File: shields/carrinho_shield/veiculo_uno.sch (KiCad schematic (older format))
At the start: 29 parts, among them J1 Conn_01x26_Male, J10 Conn_01x02_Male, J11 Conn_01x02_Male, J12 Conn_01x02_Male, J13 Conn_01x02_Male, J14 Conn_01x02_Male, J15 Conn_01x02_Male, J16 Conn_01x02_Male, J17 Conn_01x02_Male, J18 Conn_01x02_Male, J19 Conn_01x02_Male, J2 Conn_01x02_Male, J20 Conn_01x02_Male, J21 Conn_01x02_Male, J3 Conn_01x02_Male, J4 Conn_01x02_Male, J5 Conn_01x02_Male, J6 Conn_01x02_Male, J7 Conn_01x02_Male, J8 Conn_01x02_Male, J9 Conn_01x02_Male, P1 Power, P2 Analog, P3 Digital, P4 Digital, P5 CONN_01X01, P6 CONN_01X01, P7 CONN_01X01, P8 CONN_01X01

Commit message: Added shield schematic
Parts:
- removed J1: Conn_01x26_Male, Connector_PinSocket_2.54mm:PinSocket_2x13_P2.54mm_Vertical, symbol Connector:Conn_01x26_Male
- removed J7: Conn_01x02_Male, Connector_PinHeader_2.54mm:PinHeader_1x02_P2.54mm_Vertical, symbol Connector:Conn_01x02_Male
- added C1, C2: 100n, Capacitor_SMD:C_0805_2012Metric_Pad1.15x1.40mm_HandSolder, symbol pspice:CAP
- added J23: Conn_01x04_Male, Connector_PinHeader_2.54mm:PinHeader_1x04_P2.54mm_Vertical, symbol Connector:Conn_01x04_Male
- added J6: Conn_01x02_Male, Connector_PinHeader_2.54mm:PinHeader_1x02_P2.54mm_Vertical, symbol Connector:Conn_01x02_Male
- added J7: Conn_02x13_Odd_Even, Connector_PinSocket_2.54mm:PinSocket_2x13_P2.54mm_Vertical, symbol Connector_Generic:Conn_02x13_Odd_Even
- renumbered J11 to J1, J2 to J10, J4 to J11, J10 to J12, J14 to J13, J18 to J14, J19 to J16, J12 to J17, J16 to J18, J13 to J19, J5 to J2, J17 to J20, J20 to J3, J6 to J4, J8 to J5, J3 to J8
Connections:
- net labels added: AMP1, AMP2
- net labels removed: A1', A2', Conector, Conector'
- wire segments 121 -> 156
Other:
- note added: "11 - OC2A\n3 - OC2B\n\n6 - OC0A\n5- OC0B"
- note added: "2 - int0 (ext. event)\n8 - ICP1 (capture)\n\n4 - GPIO\n7 - GPIO"
- note added: "Encoder"
- moved on the sheet: J1, J10, J11, J12, J13, J14, J15, J16, J17, J18, J19, J2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

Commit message: Done PCI layout
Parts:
- removed P5: CONN_01X01, Socket_Arduino_Uno:Arduino_1pin, symbol Connector_Generic:Conn_01x01
- added D1: LED, LED_SMD:LED_0805_2012Metric, symbol Device:LED
- added R1: R, Resistor_SMD:R_0805_2012Metric, symbol Device:R
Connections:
- net +5V: now also D1.2 (A)
- net A0: now also J3.2 (Pin_2); no longer J1.2 (Pin_2)
- net A2: now also J1.2 (Pin_2); no longer J3.2 (Pin_2)
- net GND: now also J7.18 (Pin_18), R1.2
- new net: D1.1 (K), R1.1
- no-connect marks 5 -> 4
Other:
- note added: "SHIELD ARDUINO PARA CARRINHO AUTÔNOMO\nLIGAÇÃO CONFORME PLACA DE POTÊNCIA"
- note added: "Sensor optico"
- moved on the sheet: J10, J11, J12, J13, J14, J15, J16, J17, J18, J19, J20, J21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

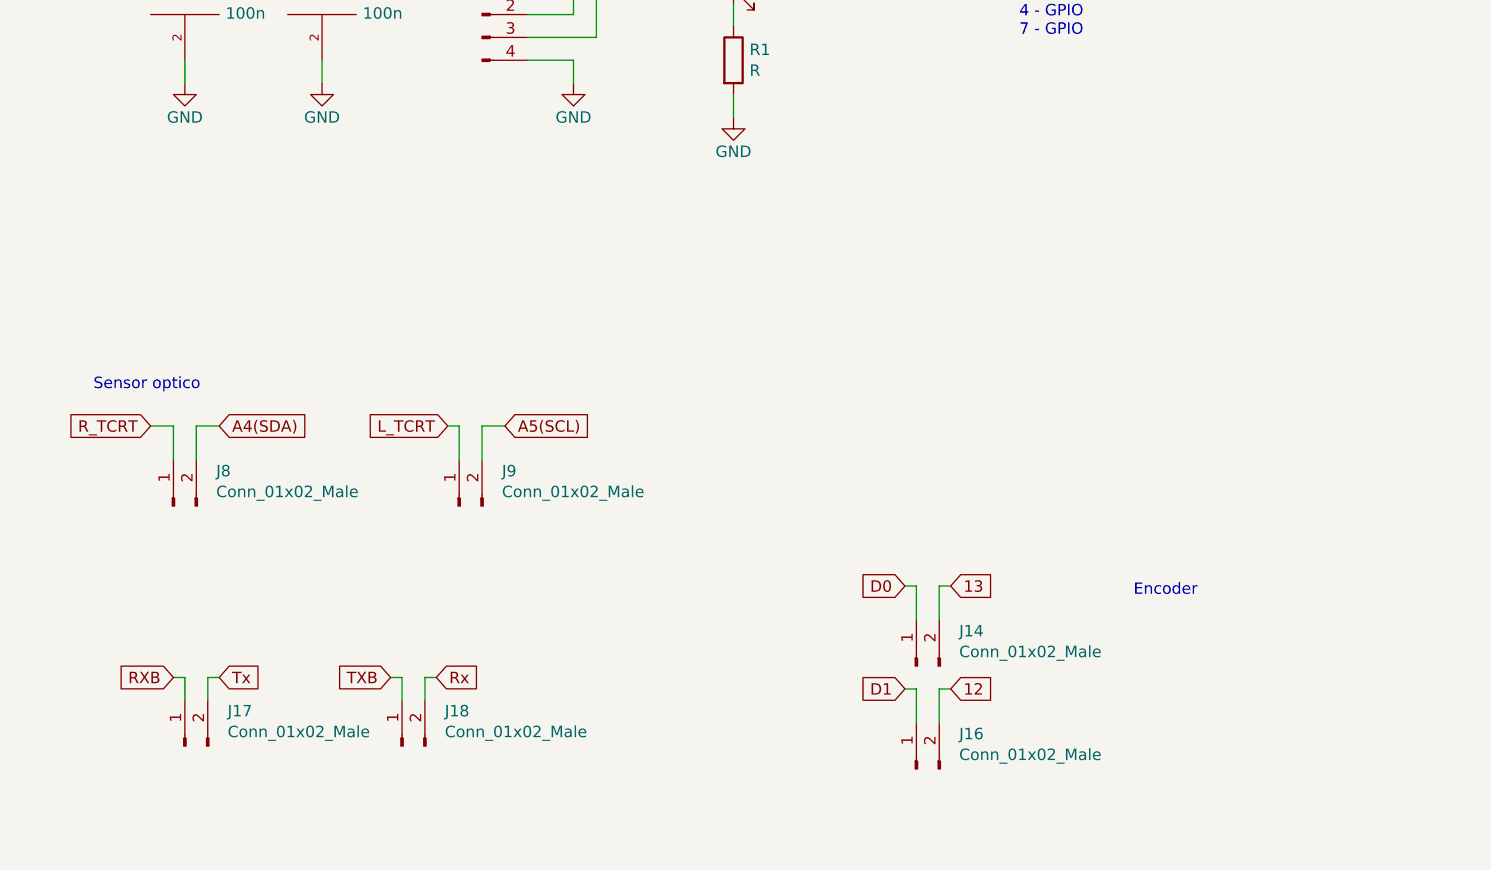
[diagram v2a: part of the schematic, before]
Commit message: Added level converter RX / TX signals
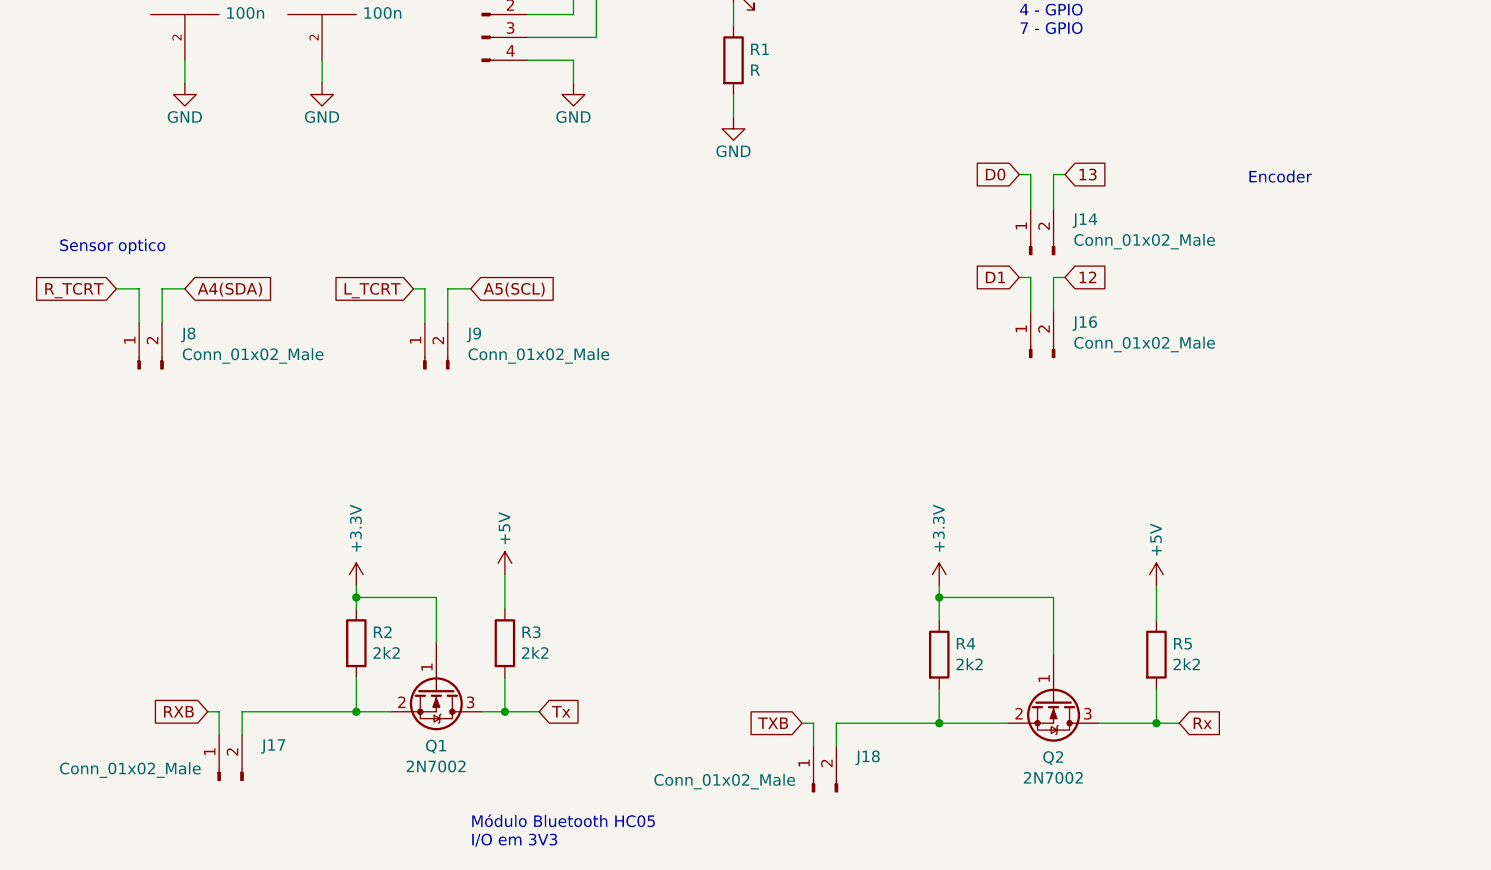
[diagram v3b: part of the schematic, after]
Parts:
- added Q1, Q2: 2N7002, Package_TO_SOT_SMD:SOT-23, symbol Transistor_FET:2N7002
- added R2, R3, R4, R5: 2k2, Resistor_SMD:R_0805_2012Metric, symbol Device:R
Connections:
- net +3V3: now also Q1.1 (G), Q2.1 (G), R2.1, R4.1
- net +5V: now also R3.1, R5.1
- net Rx: now also Q2.3 (D), R5.2; no longer J18.2 (Pin_2)
- net Tx: now also Q1.3 (D), R3.2; no longer J17.2 (Pin_2)
- new net: J18.2 (Pin_2), Q2.2 (S), R4.2
- new net: J17.2 (Pin_2), Q1.2 (S), R2.2
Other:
- note added: "Módulo Bluetooth HC05\nI/O em 3V3"
- moved on the sheet: J14, J16, J17, J18, J8, J9

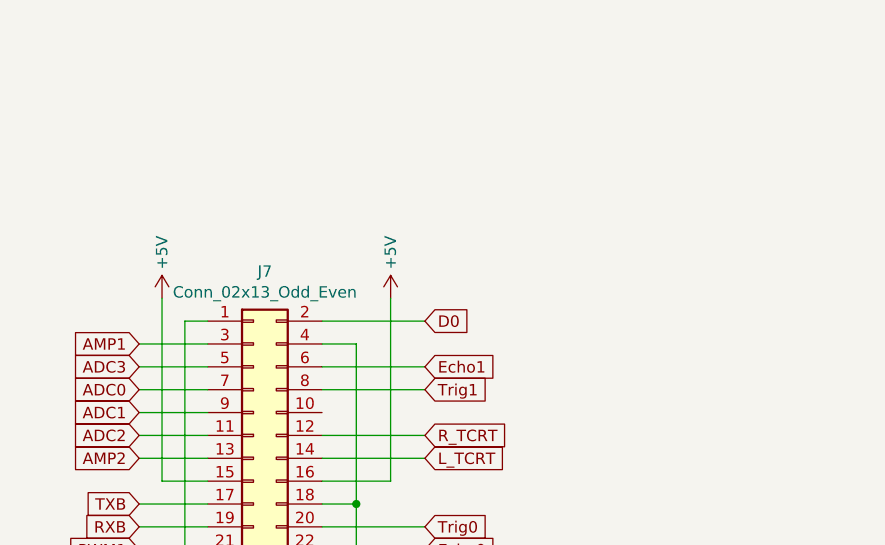
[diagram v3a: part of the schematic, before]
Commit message: Added diode in +5V.
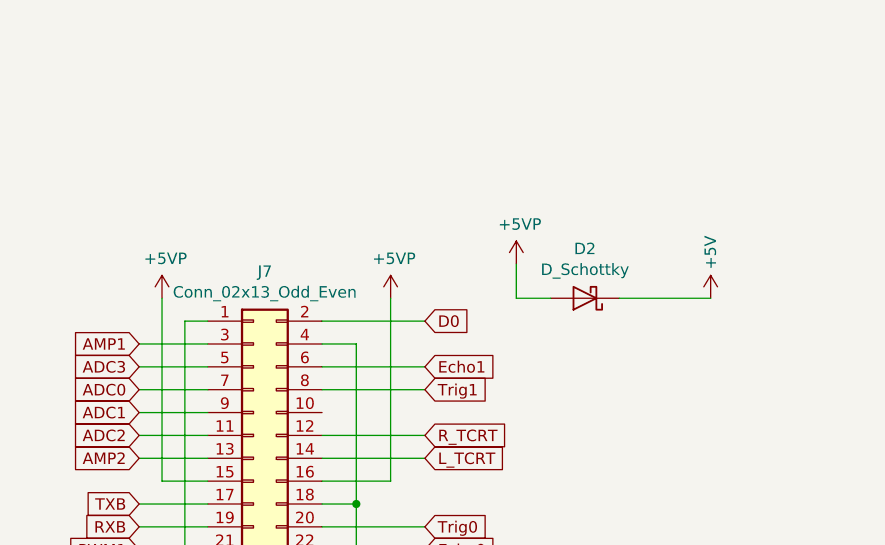
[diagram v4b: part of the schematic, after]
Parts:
- added D2: D_Schottky, Diode_SMD:D_SMB, symbol Device:D_Schottky
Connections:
- net +5V: now also D2.1 (K); no longer J7.15 (Pin_15), J7.16 (Pin_16)
- new net +5VP: D2.2 (A), J7.15 (Pin_15), J7.16 (Pin_16)
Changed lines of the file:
@@
 Wire Wire Line
 	2250 1850 2250 2550
-$Comp
-L power:+5V #PWR05
-U 1 1 5EE2252F
-P 1400 1650
-F 0 "#PWR05" H 1400 1500 50  0001 C CNN
-F 1 "+5V" V 1400 1850 50  0000 C CNN
-F 2 "" H 1400 1650 50  0000 C CNN
-F 3 "" H 1400 1650 50  0000 C CNN
-	1    1400 1650
-	1    0    0    -1
-$EndComp
-$Comp
-L power:+5V #PWR06
-U 1 1 5EE2270A
-P 2400 1650
-F 0 "#PWR06" H 2400 1500 50  0001 C CNN
-F 1 "+5V" V 2400 1850 50  0000 C CNN
-F 2 "" H 2400 1650 50  0000 C CNN
-F 3 "" H 2400 1650 50  0000 C CNN
-	1    2400 1650
-	1    0    0    -1
-$EndComp
 Wire Wire Line
 	2100 2450 2400 2450
@@
 Text Notes 2750 7700 0    50   ~ 0
 Módulo Bluetooth HC05\nI/O em 3V3
+$Comp
+L power:+5VP #PWR06
+U 1 1 5F931DB6
+P 2400 1650
+F 0 "#PWR06" H 2400 1500 50  0001 C CNN
+F 1 "+5VP" H 2415 1823 50  0000 C CNN
+F 2 "" H 2400 1650 50  0001 C CNN
+F 3 "" H 2400 1650 50  0001 C CNN
+	1    2400 1650
+	1    0    0    -1
+$EndComp
+$Comp
+L power:+5VP #PWR05
+U 1 1 5F931E0F
+P 1400 1650
+F 0 "#PWR05" H 1400 1500 50  0001 C CNN
+F 1 "+5VP" H 1415 1823 50  0000 C CNN
+F 2 "" H 1400 1650 50  0001 C CNN
+F 3 "" H 1400 1650 50  0001 C CNN
+	1    1400 1650
+	1    0    0    -1
+$EndComp
+$Comp
+L power:+5VP #PWR015
+U 1 1 5F9467DA
+P 2950 1500
+F 0 "#PWR015" H 2950 1350 50  0001 C CNN
+F 1 "+5VP" H 2965 1673 50  0000 C CNN
+F 2 "" H 2950 1500 50  0001 C CNN
+F 3 "" H 2950 1500 50  0001 C CNN
+	1    2950 1500
+	1    0    0    -1
+$EndComp
+$Comp
+L power:+5V #PWR016
+U 1 1 5F946885
+P 3800 1650
+F 0 "#PWR016" H 3800 1500 50  0001 C CNN
+F 1 "+5V" V 3800 1850 50  0000 C CNN
+F 2 "" H 3800 1650 50  0000 C CNN
+F 3 "" H 3800 1650 50  0000 C CNN
+	1    3800 1650
+	1    0    0    -1
+$EndComp
+$Comp
+L Device:D_Schottky D2
+U 1 1 5F967836
+P 3250 1650
+F 0 "D2" H 3250 1434 50  0000 C CNN
+F 1 "D_Schottky" H 3250 1525 50  0000 C CNN
+F 2 "Diode_SMD:D_SMB" H 3250 1650 50  0001 C CNN
+F 3 "~" H 3250 1650 50  0001 C CNN
+	1    3250 1650
+	-1   0    0    1
+$EndComp
+Wire Wire Line
+	3100 1650 2950 1650
+Wire Wire Line
+	2950 1650 2950 1500
+Wire Wire Line
+	3400 1650 3800 1650
 $EndSCHEMATC

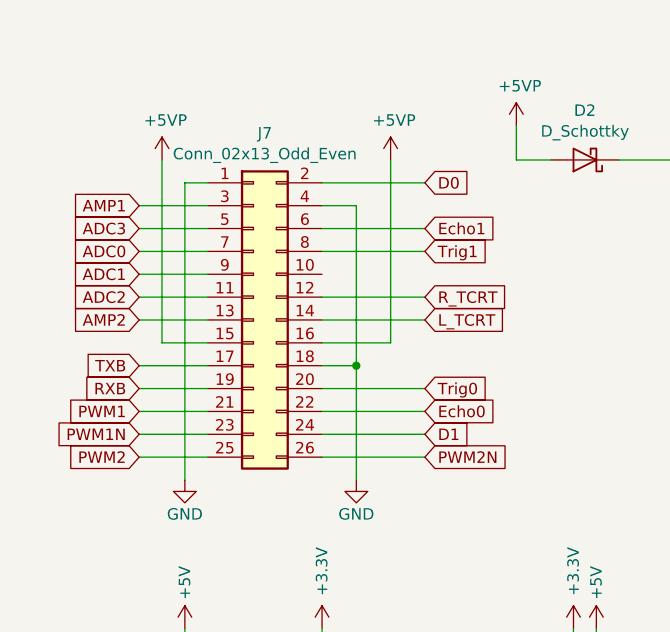
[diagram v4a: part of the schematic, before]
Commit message: Change 26 pins connector
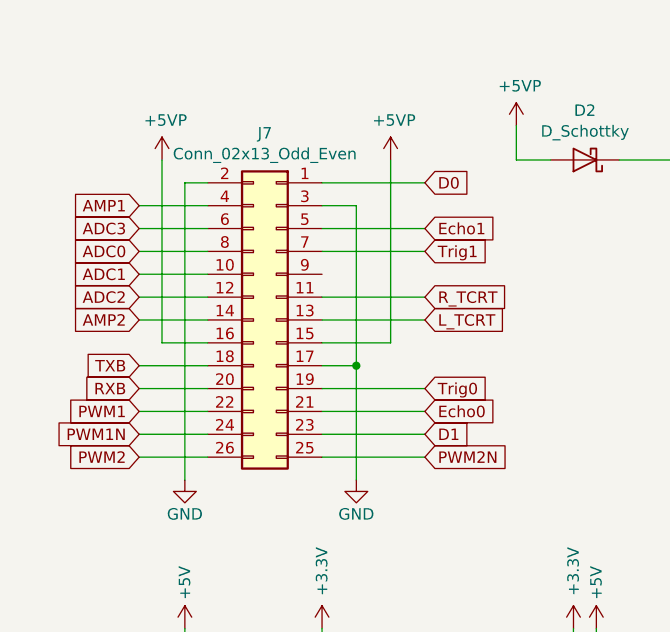
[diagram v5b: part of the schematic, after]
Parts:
- J7: footprint Connector_PinSocket_2.54mm:PinSocket_2x13_P2.54mm_Vertical -> Connector_IDC:IDC-Header_2x13_P2.54mm_Vertical
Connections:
- net ADC0: now also J7.8 (Pin_8); no longer J7.7 (Pin_7)
- net ADC1: now also J7.10 (Pin_10); no longer J7.9 (Pin_9)
- net ADC2: now also J7.12 (Pin_12); no longer J7.11 (Pin_11)
- net ADC3: now also J7.6 (Pin_6); no longer J7.5 (Pin_5)
- net AMP1: now also J7.4 (Pin_4); no longer J7.3 (Pin_3)
- net AMP2: now also J7.14 (Pin_14); no longer J7.13 (Pin_13)
- net D0: now also J7.1 (Pin_1); no longer J7.2 (Pin_2)
- net D1: now also J7.23 (Pin_23); no longer J7.24 (Pin_24)
- net Echo0: now also J7.21 (Pin_21); no longer J7.22 (Pin_22)
- net Echo1: now also J7.5 (Pin_5); no longer J7.6 (Pin_6)
- net GND: now also J7.17 (Pin_17), J7.2 (Pin_2), J7.3 (Pin_3); no longer J7.1 (Pin_1), J7.18 (Pin_18), J7.4 (Pin_4)
- net L_TCRT: now also J7.13 (Pin_13); no longer J7.14 (Pin_14)
- net PWM1: now also J7.22 (Pin_22); no longer J7.21 (Pin_21)
- net PWM1N: now also J7.24 (Pin_24); no longer J7.23 (Pin_23)
- net PWM2: now also J7.26 (Pin_26); no longer J7.25 (Pin_25)
- net PWM2N: now also J7.25 (Pin_25); no longer J7.26 (Pin_26)
- net RXB: now also J7.20 (Pin_20); no longer J7.19 (Pin_19)
- net R_TCRT: now also J7.11 (Pin_11); no longer J7.12 (Pin_12)
- net TXB: now also J7.18 (Pin_18); no longer J7.17 (Pin_17)
- net Trig0: now also J7.19 (Pin_19); no longer J7.20 (Pin_20)
- net Trig1: now also J7.7 (Pin_7); no longer J7.8 (Pin_8)
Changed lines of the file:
@@
 L Connector_Generic:Conn_02x13_Odd_Even J7
 U 1 1 5EE18C86
-P 1800 2350
-F 0 "J7" H 1850 3167 50  0000 C CNN
-F 1 "Conn_02x13_Odd_Even" H 1850 3076 50  0000 C CNN
-F 2 "Connector_PinSocket_2.54mm:PinSocket_2x13_P2.54mm_Vertical" H 1800 2350 50  0001 C CNN
-F 3 "~" H 1800 2350 50  0001 C CNN
-	1    1800 2350
-	1    0    0    -1
+P 1900 2350
+F 0 "J7" H 1950 3167 50  0000 C CNN
+F 1 "Conn_02x13_Odd_Even" H 1950 3076 50  0000 C CNN
+F 2 "Connector_IDC:IDC-Header_2x13_P2.54mm_Vertical" H 1900 2350 50  0001 C CNN
+F 3 "~" H 1900 2350 50  0001 C CNN
+	1    1900 2350
+	-1   0    0    -1
 $EndComp
 Text GLabel 2550 1750 2    50   Input ~ 0
